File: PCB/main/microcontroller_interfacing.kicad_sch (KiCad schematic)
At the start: 0 parts

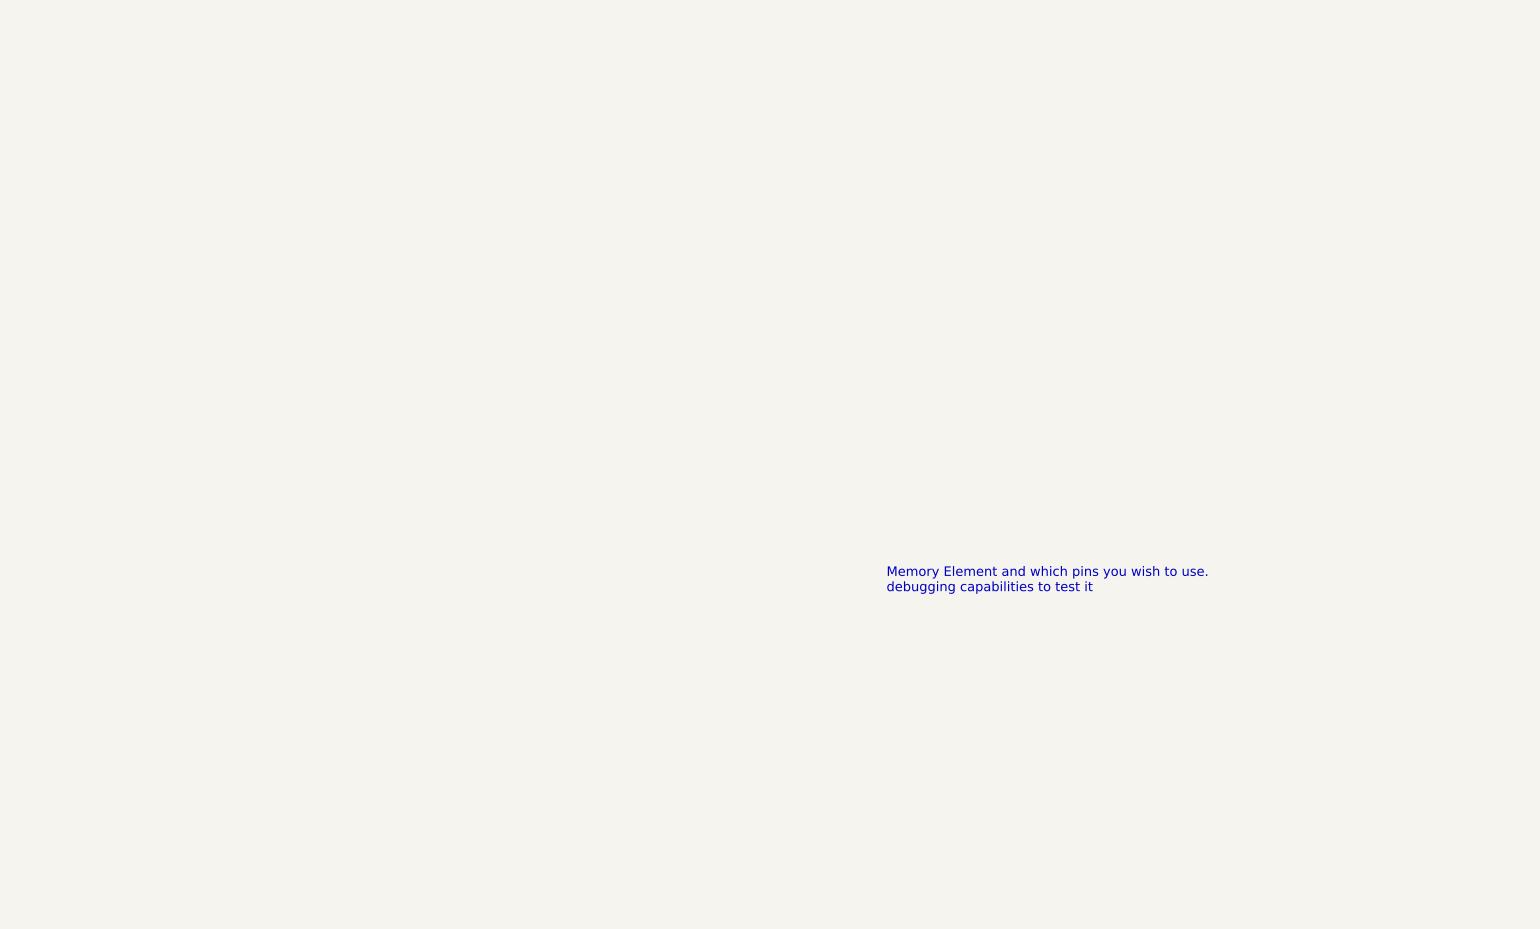
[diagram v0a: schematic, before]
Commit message: Added most of the MC interface
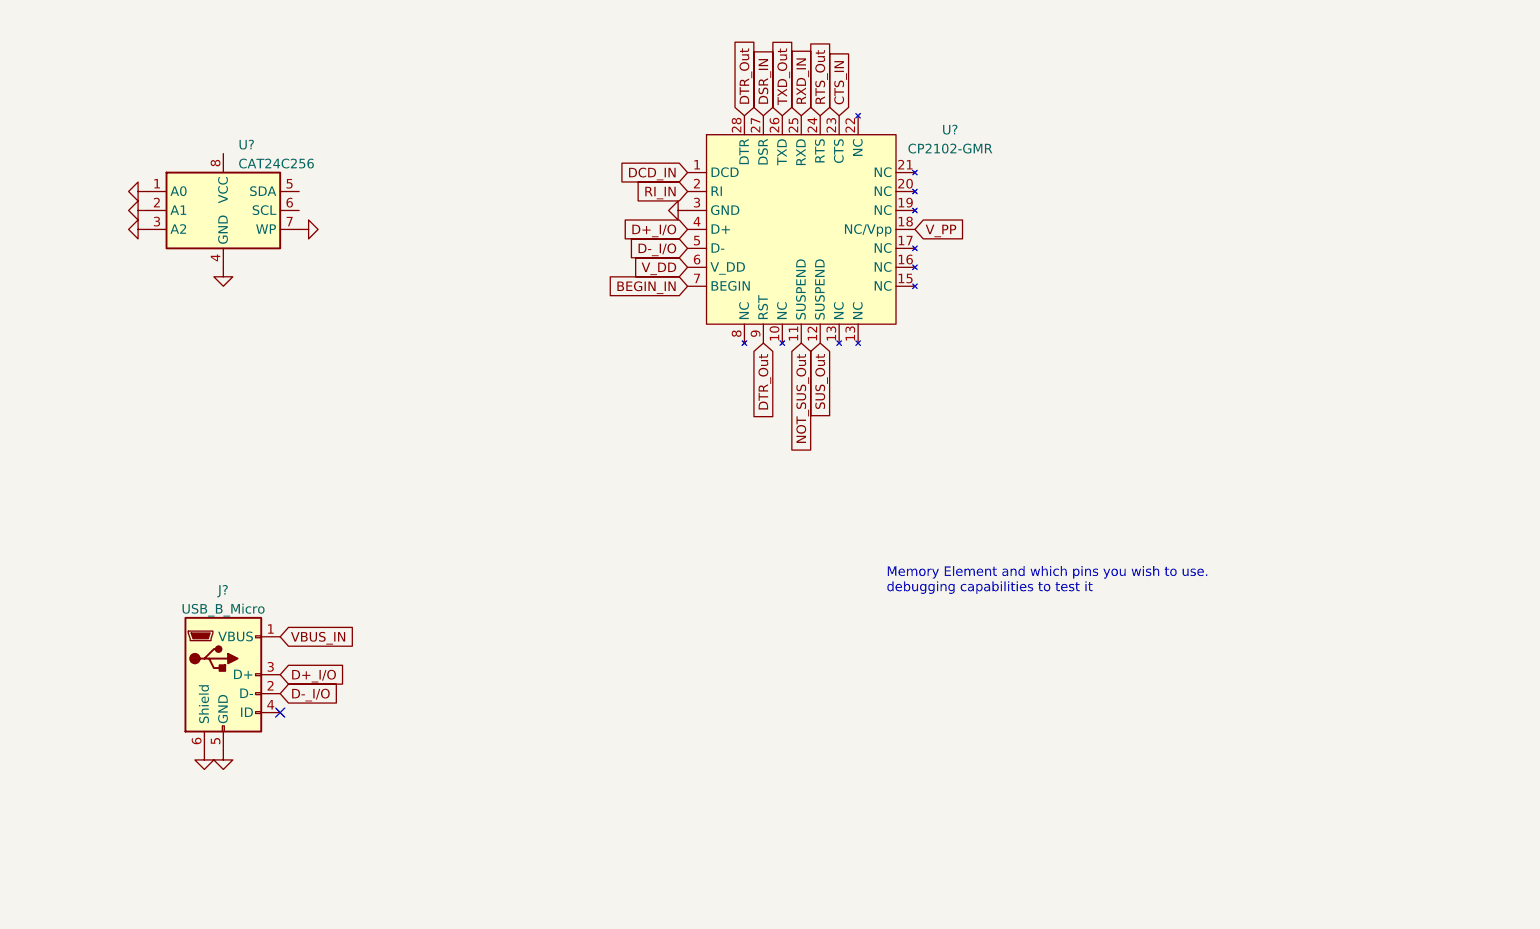
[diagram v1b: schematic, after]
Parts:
- added J?: USB_B_Micro, symbol Connector:USB_B_Micro
- added U?: CAT24C256, symbol Memory_EEPROM:CAT24C256
- added U?: CP2102-GMR, symbol custom_symbols:CP2102-GMR
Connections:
- new net BEGIN_IN: U?.7 (BEGIN)
- new net CTS_IN: U?.23 (CTS)
- new net D+_I/O: J?.3 (D+), U?.4 (D+)
- new net D-_I/O: J?.2 (D-), U?.5 (D-)
- new net DCD_IN: U?.1 (DCD)
- new net DSR_IN: U?.27 (DSR)
- new net DTR_Out: U?.28 (DTR), U?.9 (RST)
- new net GND: J?.5 (GND), J?.6 (Shield), U?.1 (A0), U?.2 (A1), U?.3 (A2), U?.3 (GND), U?.4 (GND), U?.7 (WP)
- new net NOT_SUS_Out: U?.11 (SUSPEND)
- new net RI_IN: U?.2 (RI)
- new net RTS_Out: U?.24 (RTS)
- new net RXD_IN: U?.25 (RXD)
- new net SUS_Out: U?.12 (SUSPEND)
- new net TXD_Out: U?.26 (TXD)
- new net VBUS_IN: J?.1 (VBUS)
- new net V_DD: U?.6 (V_DD)
- new net V_PP: U?.18 (NC/Vpp)
- no-connect marks 0 -> 1

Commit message: Finished v0.1 of MC Interfacing schem
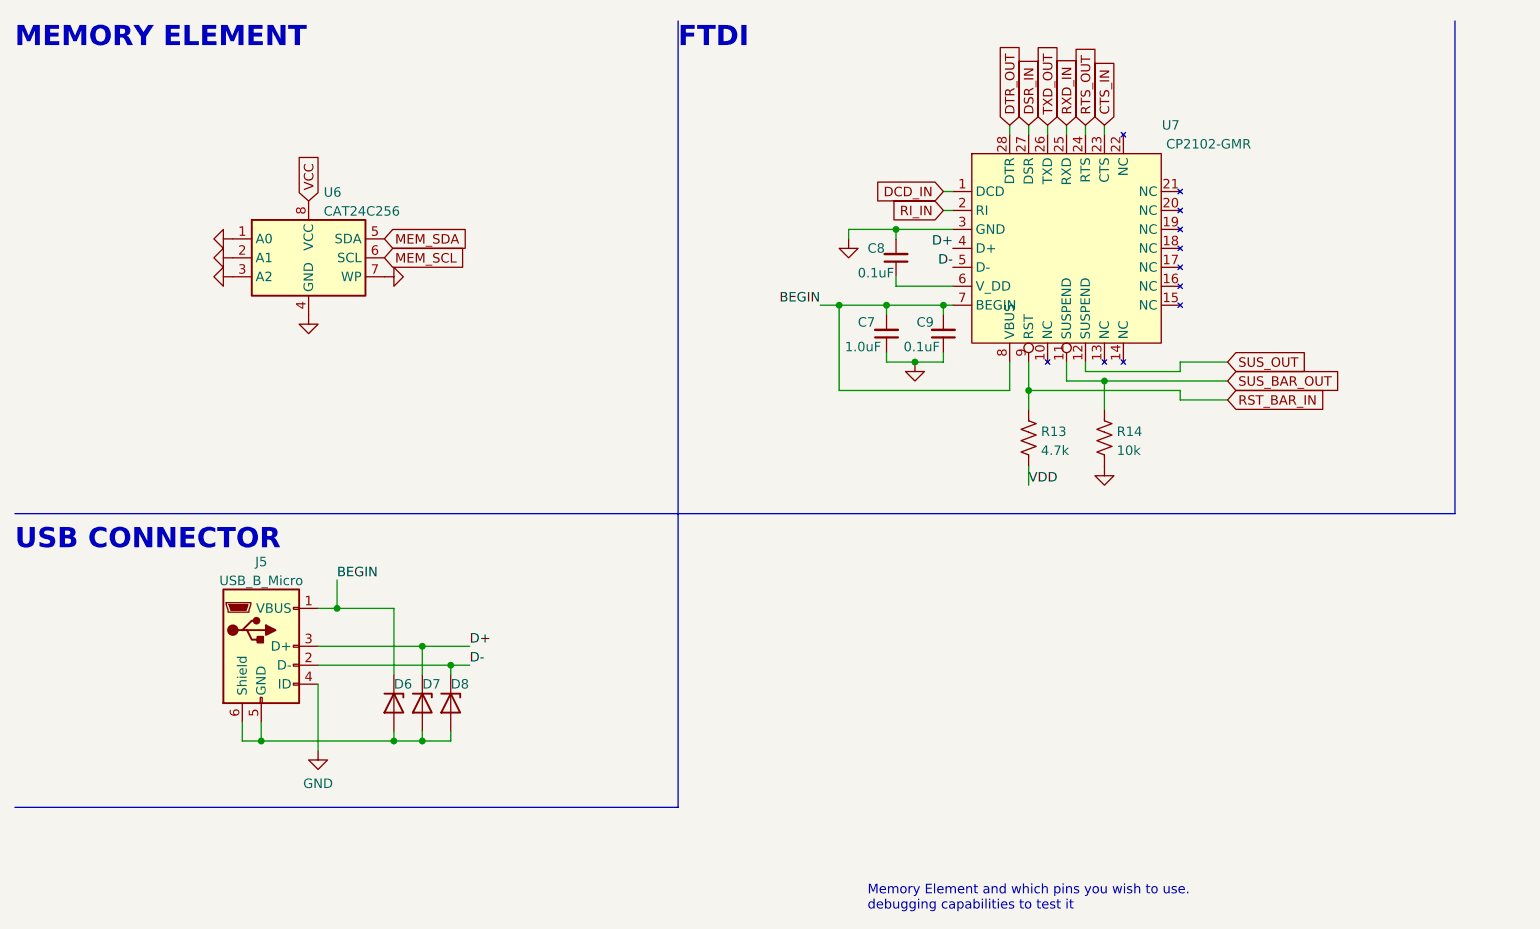
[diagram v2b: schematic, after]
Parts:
- removed U?: CP2102-GMR, symbol custom_symbols:CP2102-GMR
- added C7: 1.0uF, symbol Device:C_Small
- added C8, C9: 0.1uF, symbol Device:C_Small
- added D6, D7, D8: ZMMxx, Diode_SMD:D_MiniMELF, symbol Diode:ZMMxx
- added R13: 4.7k, symbol Device:R_US
- added R14: 10k, symbol Device:R_US
- added U7: CP2102-GMR, symbol custom_symbols:CP2102-GMR
- gave numbers to parts that had none: 2
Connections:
- net CTS_IN: now also U7.23 (CTS)
- net DCD_IN: now also U7.1 (DCD)
- net DSR_IN: now also U7.27 (DSR)
- net GND: now also J5.4 (ID), C7.1, C8.2, C9.1, R14.2, U7.3 (GND); no longer J5.5 (GND), J5.6 (Shield)
- net RI_IN: now also U7.2 (RI)
- net RXD_IN: now also U7.25 (RXD)
- net MEM_SDA: now reaches U6.5 (SDA)
- net MEM_SCL: now reaches U6.6 (SCL)
- net VCC: now reaches U6.8 (VCC)
- net D+_I/O renamed D+
- net D+: now also D7.1 (K), U7.4 (D+)
- net D-_I/O renamed D-
- net D-: now also D8.1 (K), U7.5 (D-)
- net VBUS_IN renamed BEGIN
- net BEGIN: now also C7.2, C9.2, D6.1 (K), U7.7 (BEGIN), U7.8 (VBUS)
- new net: C8.1, U7.6 (V_DD)
- new net: D6.2 (A), D7.2 (A), D8.2 (A), J5.5 (GND), J5.6 (Shield)
- new net DTR_OUT: U7.28 (DTR)
- new net RST_BAR_IN: R13.1, U7.9 (RST)
- new net RTS_OUT: U7.24 (RTS)
- new net SUS_BAR_OUT: R14.1, U7.11 (SUSPEND)
- new net SUS_OUT: U7.12 (SUSPEND)
- new net TXD_OUT: U7.26 (TXD)
- new net VDD: R13.2
- no-connect marks 1 -> 0
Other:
- note added: "FTDI"
- note added: "MEMORY ELEMENT"
- note added: "USB CONNECTOR"
- company: (none) -> EEE3088F Group 9
- title: (none) -> YNGDAV005
- moved on the sheet: J5, U6

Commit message: Updated interfacing schem
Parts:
- removed R14: 10k, symbol Device:R_US
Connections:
- net CTS_IN: no longer names the net of U7.23 (CTS)
- net DCD_IN: no longer names the net of U7.1 (DCD)
- net DSR_IN: no longer names the net of U7.27 (DSR)
- net DTR_OUT: no longer names the net of U7.28 (DTR)
- net RI_IN: no longer names the net of U7.2 (RI)
- net RST_BAR_IN renamed FTDI_RST
- net RTS_OUT: no longer names the net of U7.24 (RTS)
- net SUS_BAR_OUT: no longer names the net of U7.11 (SUSPEND)
- net SUS_OUT: no longer names the net of U7.12 (SUSPEND)
- net VCC renamed MEM_VCC
- net VDD renamed FTDI_VDD
- no-connect marks 0 -> 8
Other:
- note added: "Maybe add a button here so that we can press it to reset the FTDI device?"

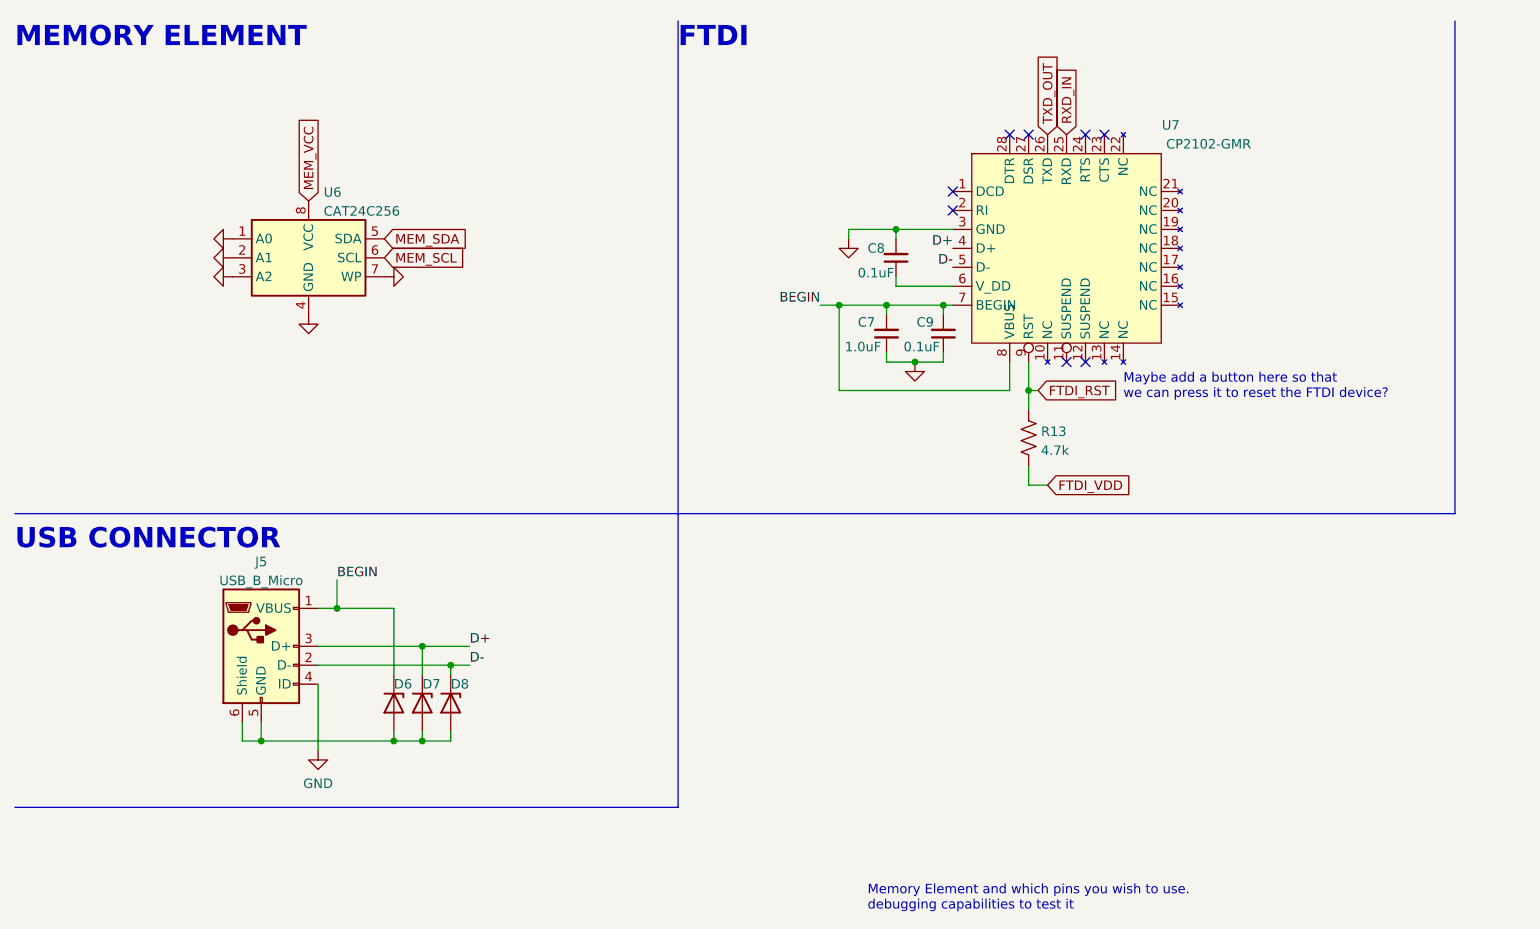
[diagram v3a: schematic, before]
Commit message: Finished initial interfacing schem
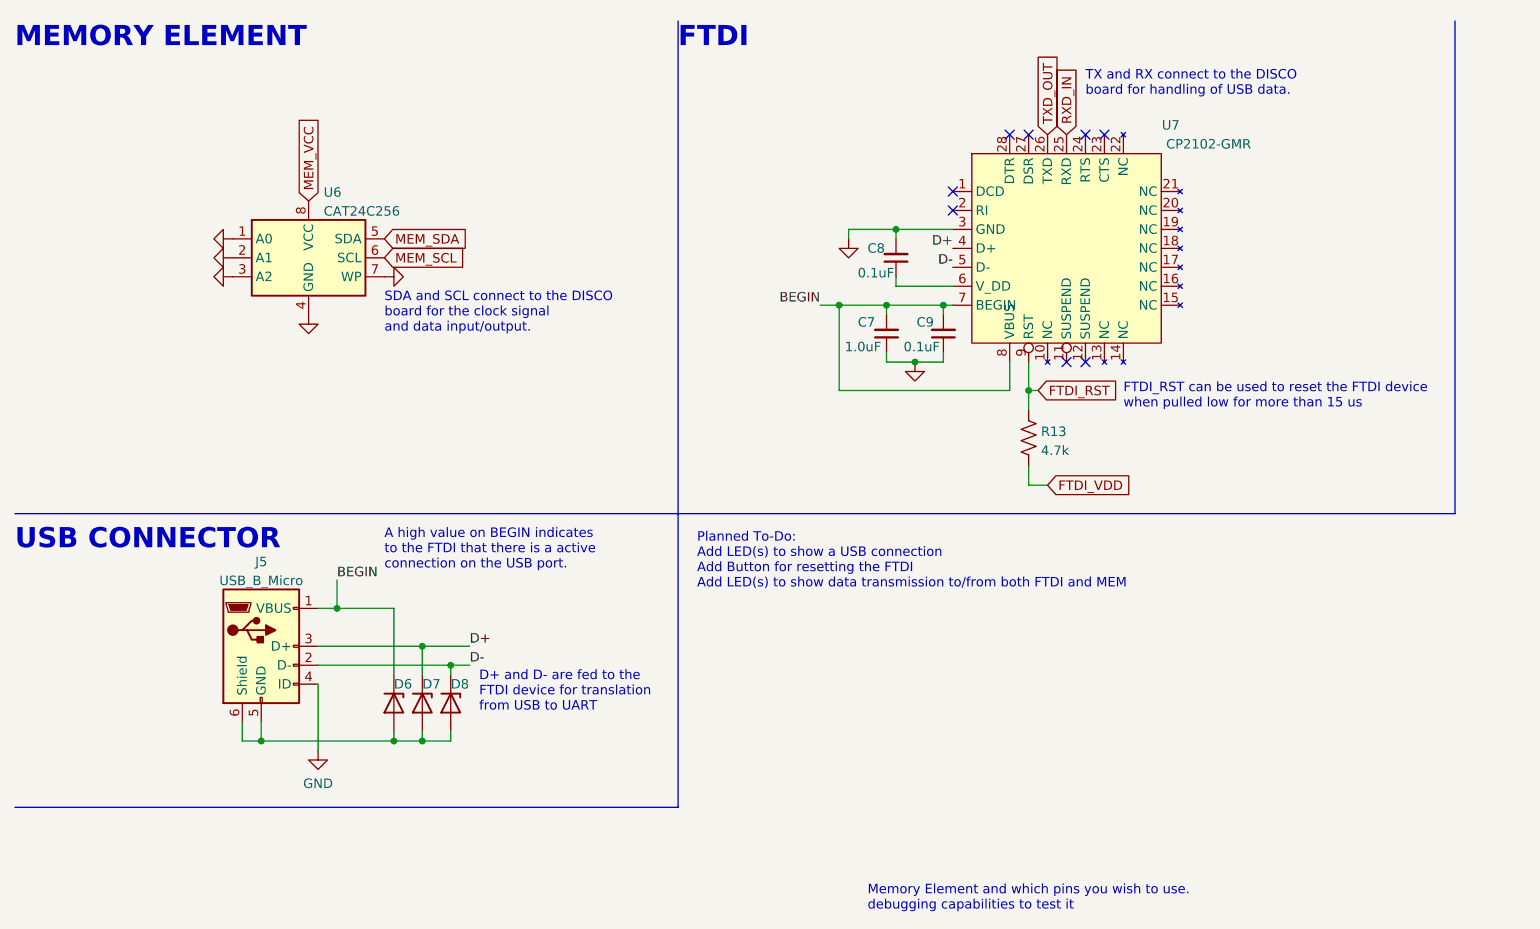
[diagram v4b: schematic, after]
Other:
- note added: "A high value on BEGIN indicates to the FTDI that there is a active connection on the USB port."
- note added: "D+ and D- are fed to the FTDI device for translation from USB to UART"
- note added: "FTDI_RST can be used to reset the FTDI device when pulled low for more than 15 us"
- note added: "Planned To-Do: Add LED(s) to show a USB connection Add Button for resetting the FTDI Add LED(s) to show data transmission to/from both FTDI and MEM"
- note added: "SDA and SCL connect to the DISCO board for the clock signal and data input/output."
- note added: "TX and RX connect to the DISCO board for handling of USB data."
- note removed: "Maybe add a button here so that we can press it to reset the FTDI device?"
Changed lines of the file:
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@@
     (stroke (width 0) (type default) (color 0 0 0 0))
+  )
+  (text "SDA and SCL connect to the DISCO\nboard for the clock signal\nand data input/output."
+    (at 62.23 54.61 0)
+    (effects (font (size 1.27 1.27)) (justify left bottom))
   )
   (text "FTDI\n" (at 101.6 16.51 0)
@@
     (effects (font (size 2.7 2.7) (thickness 0.254) bold) (justify left bottom))
   )
+  (text "TX and RX connect to the DISCO\nboard for handling of USB data."
+    (at 156.21 22.86 0)
+    (effects (font (size 1.27 1.27)) (justify left bottom))
+  )
   (text "Memory Element and which pins you wish to use.\ndebugging capabilities to test it\n"
     (at 127 132.08 0)
+    (effects (font (size 1.27 1.27)) (justify left bottom))
+  )
+  (text "A high value on BEGIN indicates\nto the FTDI that there is a active\nconnection on the USB port.\n"
+    (at 62.23 86.36 0)
+    (effects (font (size 1.27 1.27)) (justify left bottom))
+  )
+  (text "D+ and D- are fed to the\nFTDI device for translation \nfrom USB to UART"
+    (at 74.93 105.41 0)
     (effects (font (size 1.27 1.27)) (justify left bottom))
   )
@@
     (effects (font (size 2.7 2.7) (thickness 0.254) bold) (justify left bottom))
   )
-  (text "Maybe add a button here so that \nwe can press it to reset the FTDI device?\n"
-    (at 161.29 63.5 0)
+  (text "FTDI_RST can be used to reset the FTDI device\nwhen pulled low for more than 15 us "
+    (at 161.29 64.77 0)
     (effects (font (size 1.27 1.27)) (justify left bottom))
   )
+  (text "Planned To-Do:\nAdd LED(s) to show a USB connection\nAdd Button for resetting the FTDI\nAdd LED(s) to show data transmission to/from both FTDI and MEM "
+    (at 104.14 88.9 0)
+    (effects (font (size 1.27 1.27)) (justify left bottom))
+  )

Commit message: Finished initial design
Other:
- company: EEE3088F Group 9 -> University of Cape Town
- title: YNGDAV005 -> Microcontroller Interfacing Subsystem
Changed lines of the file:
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@@
   (paper "A4")
   (title_block
-    (title "YNGDAV005")
+    (title "Microcontroller Interfacing Subsystem")
     (date "2022-03-11")
     (rev "V0.2")
-    (company "EEE3088F Group 9")
-    (comment 1 "@Authors David Young")
+    (company "University of Cape Town")
+    (comment 1 "@Authors David Young (YNGDAV005)")
+    (comment 2 "@Project EEE3088F-Team-9")
   )
   (junction (at 129.54 50.8) (diameter 0) (color 0 0 0 0)
